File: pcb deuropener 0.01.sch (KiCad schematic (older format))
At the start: 30 parts, among them J1 Conn_01x02, J10 Conn_01x03, J11 Barrel_Jack_Switch, J12 Conn_01x08, J13 Conn_01x02, J14 Conn_01x02, J2 Conn_01x02, J3 Conn_01x02, J4 Conn_01x02, J8 Conn_01x02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

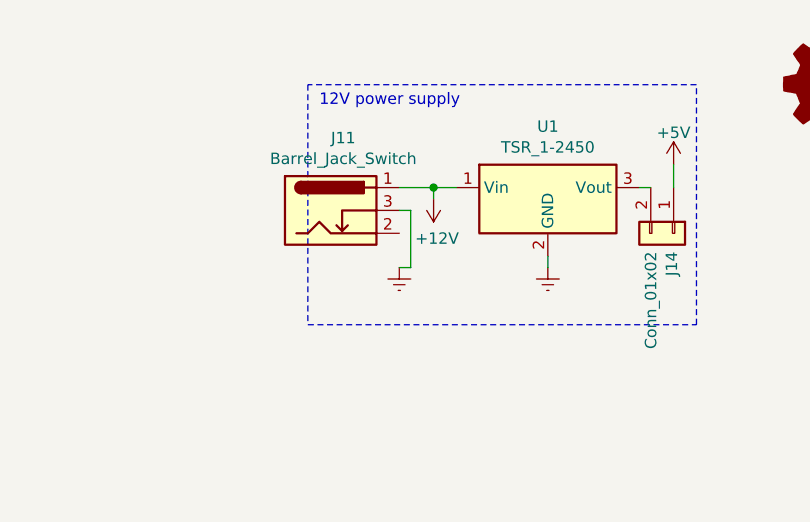
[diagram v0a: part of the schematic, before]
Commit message: Fixed: 12V barreljack connected to wrong pin #1
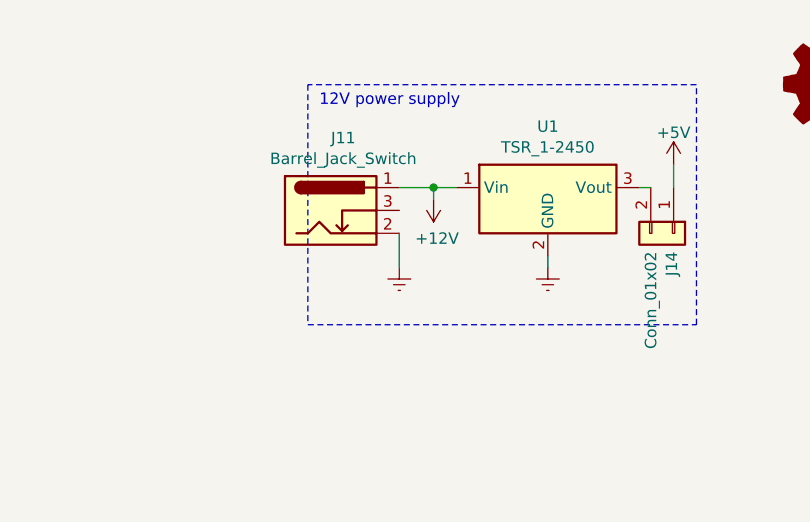
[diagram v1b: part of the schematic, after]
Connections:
- net Earth: now also J11.2; no longer J11.3
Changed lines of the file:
@@
 	1    0    0    -1
 $EndComp
-Wire Wire Line
-	8600 1600 8650 1600
-Wire Wire Line
-	8650 1600 8650 1850
-Wire Wire Line
-	8650 1850 8600 1850
 $Comp
 L Device:Q_NMOS_GDS Q1
@@
 	1    0    0    -1
 $EndComp
+Wire Wire Line
+	8600 1700 8600 1850
 $EndSCHEMATC
